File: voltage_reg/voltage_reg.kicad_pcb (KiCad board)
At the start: 2 copper layers, 46.2 x 21.6 mm, 8 parts, among them J1 USB_B_Micro, J2 Screw_Terminal_01x02, U1 AMS1117CD-3.3

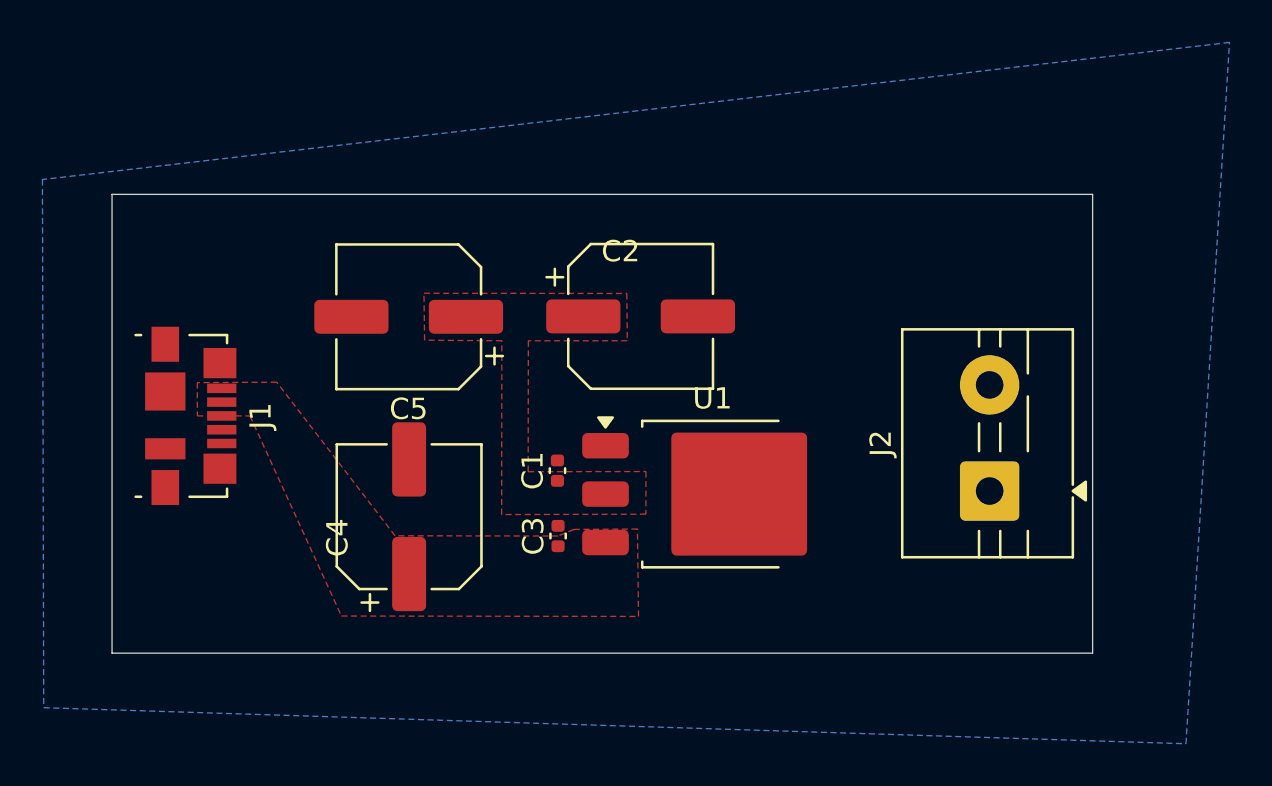
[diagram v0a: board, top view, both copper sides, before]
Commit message: finished traces and saved fabrication output files, such as gerbers and drill files, and also a 3D view in png form
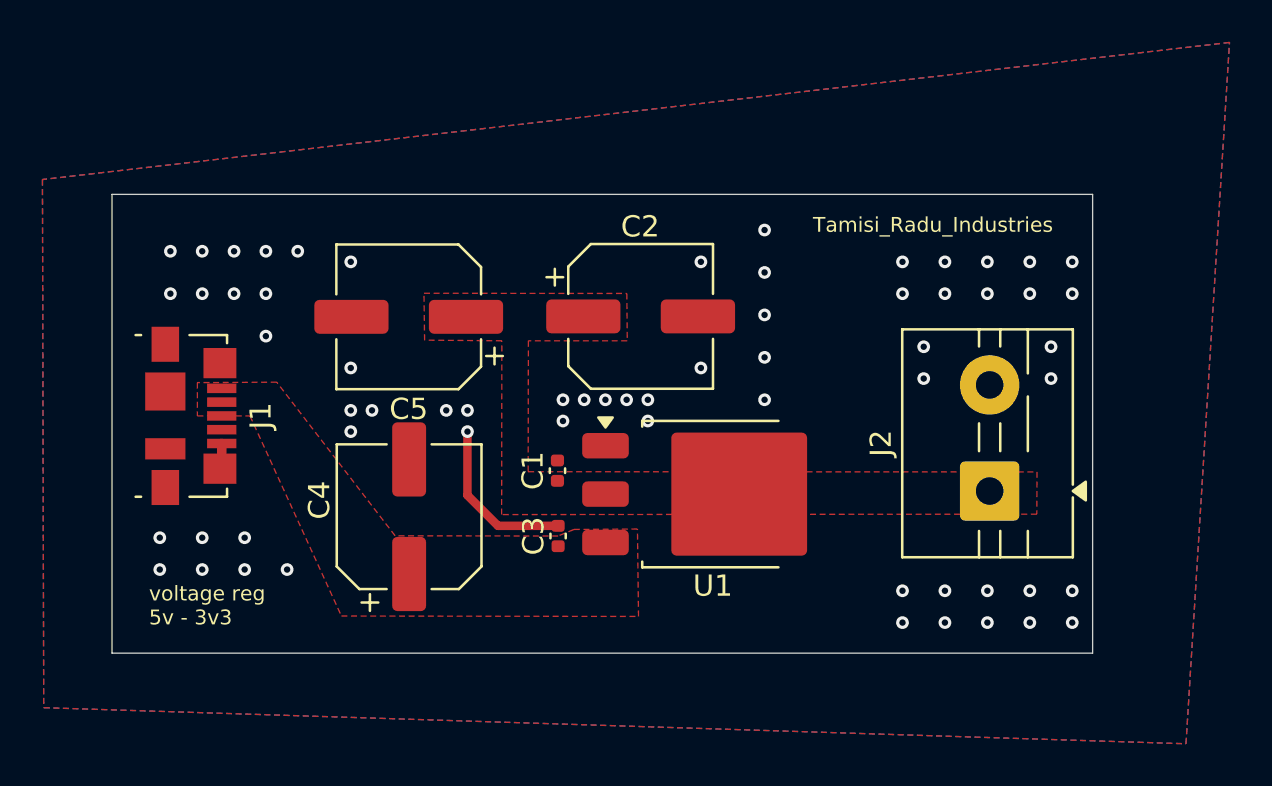
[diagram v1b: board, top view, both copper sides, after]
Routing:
- net GND: track 0.00 -> 9.09 mm, vias 0 -> 63
- added copper zone on F.Cu, net GND
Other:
- board text added: "Tamisi_Radu_Industries"
- board text added: "voltage reg 5v - 3v3"
